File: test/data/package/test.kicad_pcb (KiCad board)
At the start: 2 copper layers, 100.7 x 80 mm, 68 parts, among them P1 CONN_2, P2 CONN_2, P3 CONN_2, P4 CONN_2, P5 CONN_2, P6 CONN_2, Q1 MPSA92, Q2 MPSA42, Q3 MPSA92, Q4 MPSA42, Q5 MPSA92, Q6 MPSA42, Q7 MPSA92, Q8 MPSA42, U1 ICL7660, U2 78L05, U3 LM358N, U4 LM358N

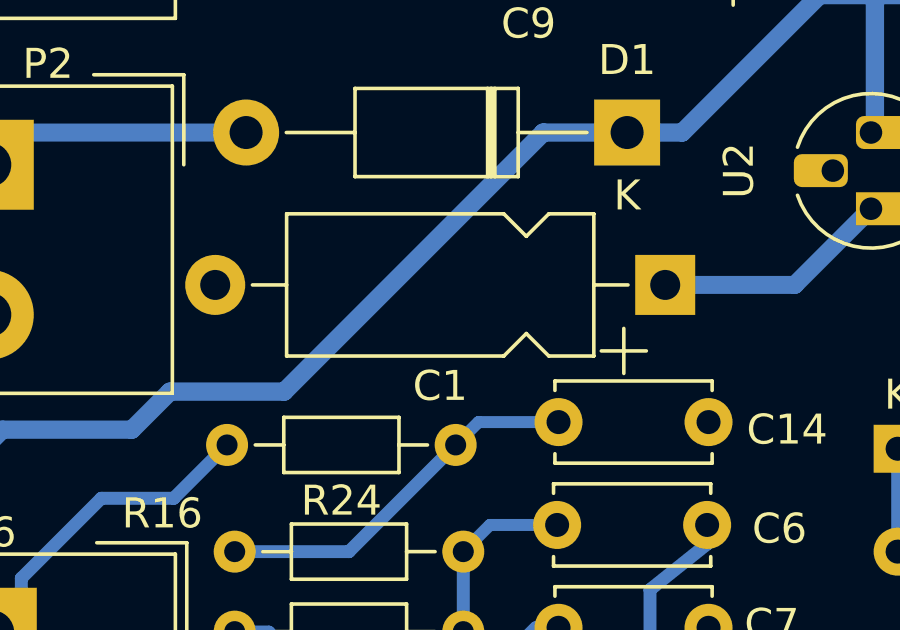
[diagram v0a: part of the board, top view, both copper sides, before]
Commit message: impl: add layout elevation,thickness query api; update: test case
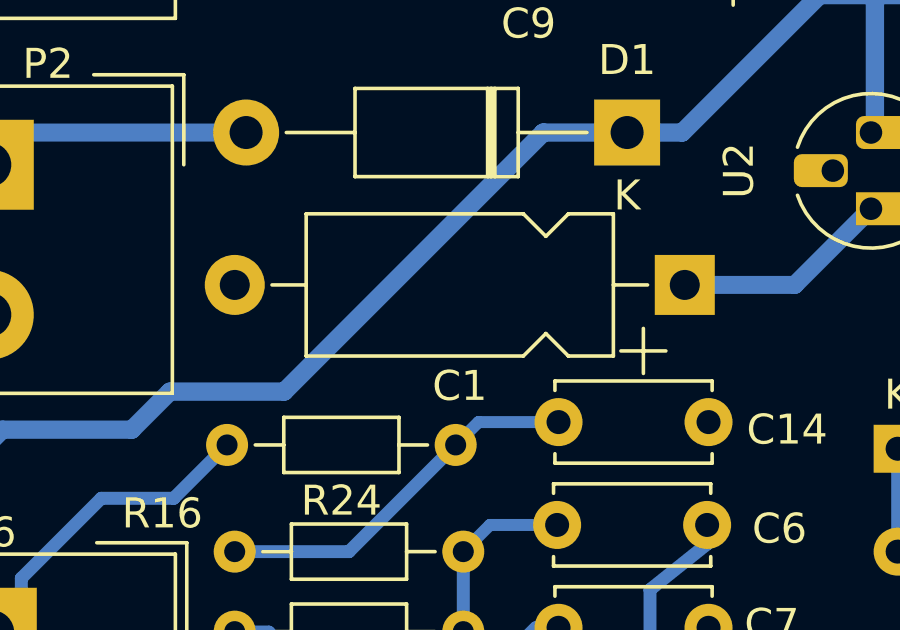
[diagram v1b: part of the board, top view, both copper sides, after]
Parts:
- moved C1 0.65 mm to (118.0, 73.4)
